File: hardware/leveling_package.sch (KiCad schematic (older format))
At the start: 18 parts, among them J1 Conn_01x16_Male, J2 Conn_01x16_Male, Q1 BSS138, SW1 SW_Push

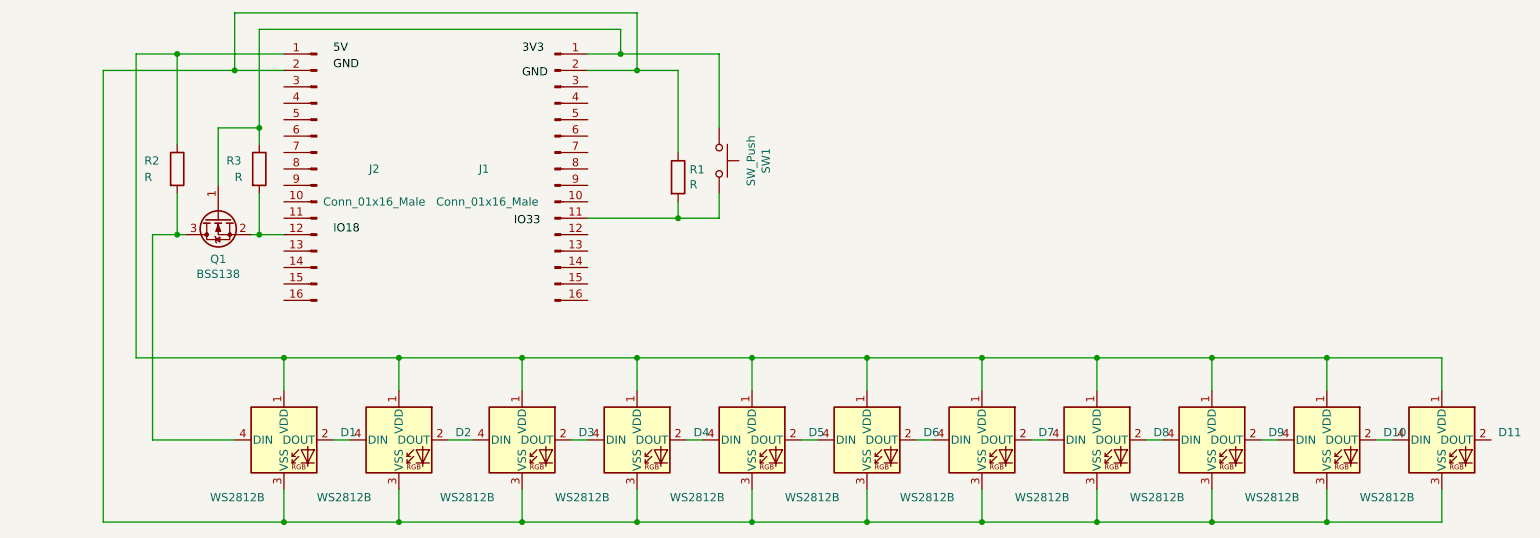
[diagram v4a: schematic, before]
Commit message: added proto solder pads
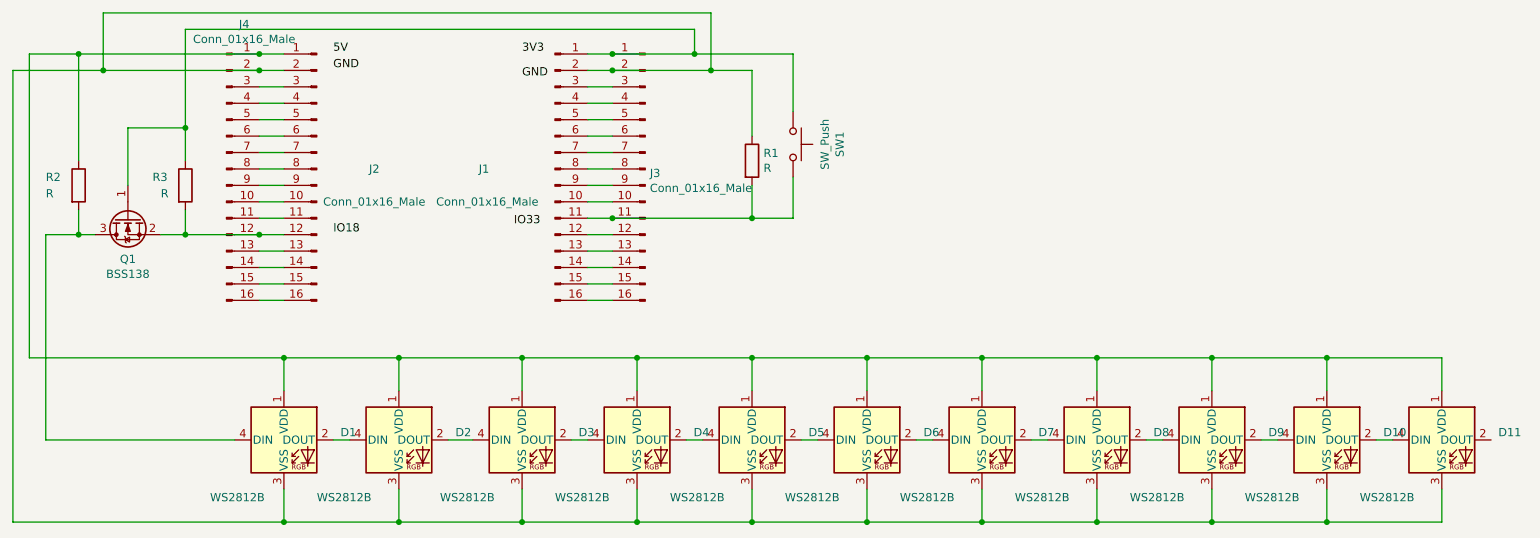
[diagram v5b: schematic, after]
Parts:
- added J3, J4: Conn_01x16_Male, Connector_PinHeader_2.54mm:PinHeader_1x16_P2.54mm_Vertical, symbol Connector:Conn_01x16_Male
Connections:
- net at D1.1 (VDD), D10.1 (VDD), D11.1 (VDD)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: now also J4.1 (Pin_1)
- net at J2.10 (Pin_10): now also J4.10 (Pin_10)
- net at J2.11 (Pin_11): now also J4.11 (Pin_11)
- net at J2.12 (Pin_12), Q1.2 (S), R3.2: now also J4.12 (Pin_12)
- net at J2.13 (Pin_13): now also J4.13 (Pin_13)
- net at J2.14 (Pin_14): now also J4.14 (Pin_14)
- net at J2.15 (Pin_15): now also J4.15 (Pin_15)
- net at J2.16 (Pin_16): now also J4.16 (Pin_16)
- net at D1.3 (VSS), D10.3 (VSS), D11.3 (VSS)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: now also J3.2 (Pin_2), J4.2 (Pin_2)
- net at J2.3 (Pin_3): now also J4.3 (Pin_3)
- net at J2.4 (Pin_4): now also J4.4 (Pin_4)
- net at J2.5 (Pin_5): now also J4.5 (Pin_5)
- net at J2.6 (Pin_6): now also J4.6 (Pin_6)
- net at J2.7 (Pin_7): now also J4.7 (Pin_7)
- net at J2.8 (Pin_8): now also J4.8 (Pin_8)
- net at J2.9 (Pin_9): now also J4.9 (Pin_9)
- net at J1.1 (Pin_1), Q1.1 (G), R3.1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: now also J3.1 (Pin_1)
- net at J1.10 (Pin_10): now also J3.10 (Pin_10)
- net at J1.11 (Pin_11), R1.2, SW1.2: now also J3.11 (Pin_11)
- net at J1.12 (Pin_12): now also J3.12 (Pin_12)
- net at J1.13 (Pin_13): now also J3.13 (Pin_13)
- net at J1.14 (Pin_14): now also J3.14 (Pin_14)
- net at J1.15 (Pin_15): now also J3.15 (Pin_15)
- net at J1.16 (Pin_16): now also J3.16 (Pin_16)
- net at J1.3 (Pin_3): now also J3.3 (Pin_3)
- net at J1.4 (Pin_4): now also J3.4 (Pin_4)
- net at J1.5 (Pin_5): now also J3.5 (Pin_5)
- net at J1.6 (Pin_6): now also J3.6 (Pin_6)
- net at J1.7 (Pin_7): now also J3.7 (Pin_7)
- net at J1.8 (Pin_8): now also J3.8 (Pin_8)
- net at J1.9 (Pin_9): now also J3.9 (Pin_9)
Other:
- moved on the sheet: Q1, R1, R2, R3, SW1
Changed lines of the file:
@@
 L Switch:SW_Push SW1
 U 1 1 603FB7A3
-P 6100 3300
-F 0 "SW1" H 6100 3585 50  0000 C CNN
-F 1 "SW_Push" H 6100 3494 50  0000 C CNN
-F 2 "Button_Switch_THT:SW_PUSH_6mm" H 6100 3500 50  0001 C CNN
-F 3 "~" H 6100 3500 50  0001 C CNN
-	1    6100 3300
+P 6550 3200
+F 0 "SW1" H 6550 3485 50  0000 C CNN
+F 1 "SW_Push" H 6550 3394 50  0000 C CNN
+F 2 "Button_Switch_THT:SW_PUSH_6mm" H 6550 3400 50  0001 C CNN
+F 3 "~" H 6550 3400 50  0001 C CNN
+	1    6550 3200
 	0    1    1    0
 $EndComp
@@
 L Device:R R1
 U 1 1 603F0D7F
-P 5850 3400
-F 0 "R1" H 5920 3446 50  0000 L CNN
-F 1 "R" H 5920 3355 50  0000 L CNN
-F 2 "Resistor_SMD:R_0805_2012Metric_Pad1.15x1.40mm_HandSolder" V 5780 3400 50  0001 C CNN
-F 3 "~" H 5850 3400 50  0001 C CNN
-	1    5850 3400
-	1    0    0    -1
-$EndComp
-Wire Wire Line
-	5300 3650 5850 3650
-Wire Wire Line
-	5850 3650 5850 3550
-Wire Wire Line
-	5850 3250 5850 2750
-Wire Wire Line
-	5850 2750 5600 2750
-Wire Wire Line
-	5850 3650 6100 3650
-Wire Wire Line
-	6100 3650 6100 3500
-Connection ~ 5850 3650
-Wire Wire Line
-	6100 3100 6100 2650
-Wire Wire Line
-	6100 2650 5500 2650
+P 6300 3300
+F 0 "R1" H 6370 3346 50  0000 L CNN
+F 1 "R" H 6370 3255 50  0000 L CNN
+F 2 "Resistor_SMD:R_0805_2012Metric_Pad1.15x1.40mm_HandSolder" V 6230 3300 50  0001 C CNN
+F 3 "~" H 6300 3300 50  0001 C CNN
+	1    6300 3300
+	1    0    0    -1
+$EndComp
+Wire Wire Line
+	5300 3650 5450 3650
+Wire Wire Line
+	6300 3650 6300 3450
+Wire Wire Line
+	6300 3150 6300 2750
+Wire Wire Line
+	6550 3650 6550 3400
+Connection ~ 6300 3650
+Wire Wire Line
+	6550 3000 6550 2650
 Wire Wire Line
 	3450 4700 3450 4500
 Wire Wire Line
-	3450 4500 2550 4500
-Wire Wire Line
-	2550 4500 2550 2650
-Wire Wire Line
-	2550 2650 2800 2650
+	3450 4500 1900 4500
+Wire Wire Line
+	1900 4500 1900 2650
 Wire Wire Line
 	3450 5300 3450 5500
 Wire Wire Line
-	3450 5500 2350 5500
-Wire Wire Line
-	2350 5500 2350 2750
-Wire Wire Line
-	2350 2750 3150 2750
+	3450 5500 1800 5500
+Wire Wire Line
+	1800 5500 1800 2750
+Wire Wire Line
+	1800 2750 2350 2750
 $Comp
 L Transistor_FET:BSS138 Q1
 U 1 1 6040B788
-P 3050 3650
-F 0 "Q1" V 3299 3650 50  0000 C CNN
-F 1 "BSS138" V 3390 3650 50  0000 C CNN
-F 2 "Package_TO_SOT_SMD:SOT-23" H 3250 3575 50  0001 L CIN
-F 3 "https://www.fairchildsemi.com/datasheets/BS/BSS138.pdf" H 3050 3650 50  0001 L CNN
-	1    3050 3650
+P 2500 3650
+F 0 "Q1" V 2749 3650 50  0000 C CNN
+F 1 "BSS138" V 2840 3650 50  0000 C CNN
+F 2 "Package_TO_SOT_SMD:SOT-23" H 2700 3575 50  0001 L CIN
+F 3 "https://www.fairchildsemi.com/datasheets/BS/BSS138.pdf" H 2500 3650 50  0001 L CNN
+	1    2500 3650
 	0    -1   1    0
 $EndComp
@@
 	3450 3750 3300 3750
 Wire Wire Line
-	3150 5000 2650 5000
-Wire Wire Line
-	2650 5000 2650 3750
-Wire Wire Line
-	2650 3750 2800 3750
+	3150 5000 2000 5000
+Wire Wire Line
+	2000 5000 2000 3750
+Wire Wire Line
+	2000 3750 2200 3750
 $Comp
 L Device:R R3
 U 1 1 6043545A
-P 3300 3350
-F 0 "R3" H 3100 3400 50  0000 L CNN
-F 1 "R" H 3150 3300 50  0000 L CNN
-F 2 "Resistor_SMD:R_0805_2012Metric_Pad1.15x1.40mm_HandSolder" V 3230 3350 50  0001 C CNN
-F 3 "~" H 3300 3350 50  0001 C CNN
-	1    3300 3350
-	1    0    0    -1
-$EndComp
-Wire Wire Line
-	3300 3500 3300 3750
-Connection ~ 3300 3750
-Wire Wire Line
-	3300 3750 3250 3750
-Wire Wire Line
-	3300 3200 3300 3100
-Wire Wire Line
-	3300 2500 5500 2500
-Wire Wire Line
-	5500 2500 5500 2650
-Connection ~ 5500 2650
-Wire Wire Line
-	5500 2650 5300 2650
-Wire Wire Line
-	3300 3100 3050 3100
-Wire Wire Line
-	3050 3100 3050 3450
-Connection ~ 3300 3100
-Wire Wire Line
-	3300 3100 3300 2500
+P 2850 3450
+F 0 "R3" H 2650 3500 50  0000 L CNN
+F 1 "R" H 2700 3400 50  0000 L CNN
+F 2 "Resistor_SMD:R_0805_2012Metric_Pad1.15x1.40mm_HandSolder" V 2780 3450 50  0001 C CNN
+F 3 "~" H 2850 3450 50  0001 C CNN
+	1    2850 3450
+	1    0    0    -1
+$EndComp
+Wire Wire Line
+	2850 3600 2850 3750
+Connection ~ 2850 3750
+Wire Wire Line
+	2850 3750 2700 3750
+Wire Wire Line
+	2850 3300 2850 3100
+Wire Wire Line
+	5950 2500 5950 2650
+Connection ~ 5950 2650
+Wire Wire Line
+	5950 2650 5450 2650
+Connection ~ 2850 3100
+Wire Wire Line
+	2850 3100 2850 2500
 $Comp
 L Device:R R2
 U 1 1 604443A8
-P 2800 3350
-F 0 "R2" H 2600 3400 50  0000 L CNN
-F 1 "R" H 2600 3300 50  0000 L CNN
-F 2 "Resistor_SMD:R_0805_2012Metric_Pad1.15x1.40mm_HandSolder" V 2730 3350 50  0001 C CNN
-F 3 "~" H 2800 3350 50  0001 C CNN
-	1    2800 3350
-	1    0    0    -1
-$EndComp
-Wire Wire Line
-	2800 3500 2800 3750
-Connection ~ 2800 3750
-Wire Wire Line
-	2800 3750 2850 3750
-Wire Wire Line
-	2800 3200 2800 2650
-Connection ~ 2800 2650
-Wire Wire Line
-	2800 2650 3450 2650
+P 2200 3450
+F 0 "R2" H 2000 3500 50  0000 L CNN
+F 1 "R" H 2000 3400 50  0000 L CNN
+F 2 "Resistor_SMD:R_0805_2012Metric_Pad1.15x1.40mm_HandSolder" V 2130 3450 50  0001 C CNN
+F 3 "~" H 2200 3450 50  0001 C CNN
+	1    2200 3450
+	1    0    0    -1
+$EndComp
+Wire Wire Line
+	2200 3600 2200 3750
+Connection ~ 2200 3750
+Wire Wire Line
+	2200 3750 2300 3750
+Wire Wire Line
+	2200 3300 2200 2650
 $Comp
 L LED:WS2812B D2
@@
 	10100 5000 10200 5000
 Wire Wire Line
-	3150 2750 3150 2400
-Wire Wire Line
-	3150 2400 5600 2400
-Wire Wire Line
-	5600 2400 5600 2750
-Connection ~ 3150 2750
-Wire Wire Line
-	3150 2750 3450 2750
-Connection ~ 5600 2750
-Wire Wire Line
-	5600 2750 5300 2750
+	2350 2750 2350 2400
+Wire Wire Line
+	6050 2400 6050 2750
+Connection ~ 2350 2750
+Wire Wire Line
+	2350 2750 3300 2750
+Connection ~ 6050 2750
+Wire Wire Line
+	6050 2750 5450 2750
+Wire Wire Line
+	5950 2650 6550 2650
+Wire Wire Line
+	6300 3650 6550 3650
+Wire Wire Line
+	6050 2750 6300 2750
+$Comp
+L Connector:Conn_01x16_Male J3
+U 1 1 604600F5
+P 5650 3350
+F 0 "J3" H 5622 3324 50  0000 R CNN
+F 1 "Conn_01x16_Male" H 5622 3233 50  0000 R CNN
+F 2 "Connector_PinHeader_2.54mm:PinHeader_1x16_P2.54mm_Vertical" H 5650 3350 50  0001 C CNN
+F 3 "~" H 5650 3350 50  0001 C CNN
+	1    5650 3350
+	-1   0    0    -1
+$EndComp
+Connection ~ 5450 2650
+Wire Wire Line
+	5450 2650 5300 2650
+Connection ~ 5450 3650
+Wire Wire Line
+	5450 3650 6300 3650
+Connection ~ 5450 2750
+Wire Wire Line
+	5450 2750 5300 2750
+Wire Wire Line
+	5300 2850 5450 2850
+Wire Wire Line
+	5300 2950 5450 2950
+Wire Wire Line
+	5300 3050 5450 3050
+Wire Wire Line
+	5300 3150 5450 3150
+Wire Wire Line
+	5300 3250 5450 3250
+Wire Wire Line
+	5300 3350 5450 3350
+Wire Wire Line
+	5300 3450 5450 3450
+Wire Wire Line
+	5300 3550 5450 3550
+Wire Wire Line
+	5300 3750 5450 3750
+Wire Wire Line
+	5300 3850 5450 3850
+Wire Wire Line
+	5300 3950 5450 3950
+Wire Wire Line
+	5300 4050 5450 4050
+Wire Wire Line
+	5300 4150 5450 4150
+Wire Wire Line
+	2200 2650 3300 2650
+Wire Wire Line
+	1900 2650 2200 2650
+Connection ~ 2200 2650
+Wire Wire Line
+	2350 2400 6050 2400
+Wire Wire Line
+	2500 3100 2500 3450
+Wire Wire Line
+	2500 3100 2850 3100
+Wire Wire Line
+	2850 2500 5950 2500
+$Comp
+L Connector:Conn_01x16_Male J4
+U 1 1 605170FC
+P 3100 3350
+F 0 "J4" H 3208 4231 50  0000 C CNN
+F 1 "Conn_01x16_Male" H 3208 4140 50  0000 C CNN
+F 2 "Connector_PinHeader_2.54mm:PinHeader_1x16_P2.54mm_Vertical" H 3100 3350 50  0001 C CNN
+F 3 "~" H 3100 3350 50  0001 C CNN
+	1    3100 3350
+	1    0    0    -1
+$EndComp
+Connection ~ 3300 2650
+Wire Wire Line
+	3300 2650 3450 2650
+Connection ~ 3300 3750
+Wire Wire Line
+	3300 3750 2850 3750
+Connection ~ 3300 2750
+Wire Wire Line
+	3300 2750 3450 2750
+Wire Wire Line
+	3300 2850 3450 2850
+Wire Wire Line
+	3450 2950 3300 2950
+Wire Wire Line
+	3300 3050 3450 3050
+Wire Wire Line
+	3450 3150 3300 3150
+Wire Wire Line
+	3300 3250 3450 3250
+Wire Wire Line
+	3450 3350 3300 3350
+Wire Wire Line
+	3300 3450 3450 3450
+Wire Wire Line
+	3450 3550 3300 3550
+Wire Wire Line
+	3300 3650 3450 3650
+Wire Wire Line
+	3450 3850 3300 3850
+Wire Wire Line
+	3300 3950 3450 3950
+Wire Wire Line
+	3450 4050 3300 4050
+Wire Wire Line
+	3300 4150 3450 4150
 $EndSCHEMATC
